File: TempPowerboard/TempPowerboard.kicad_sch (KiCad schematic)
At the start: 0 parts

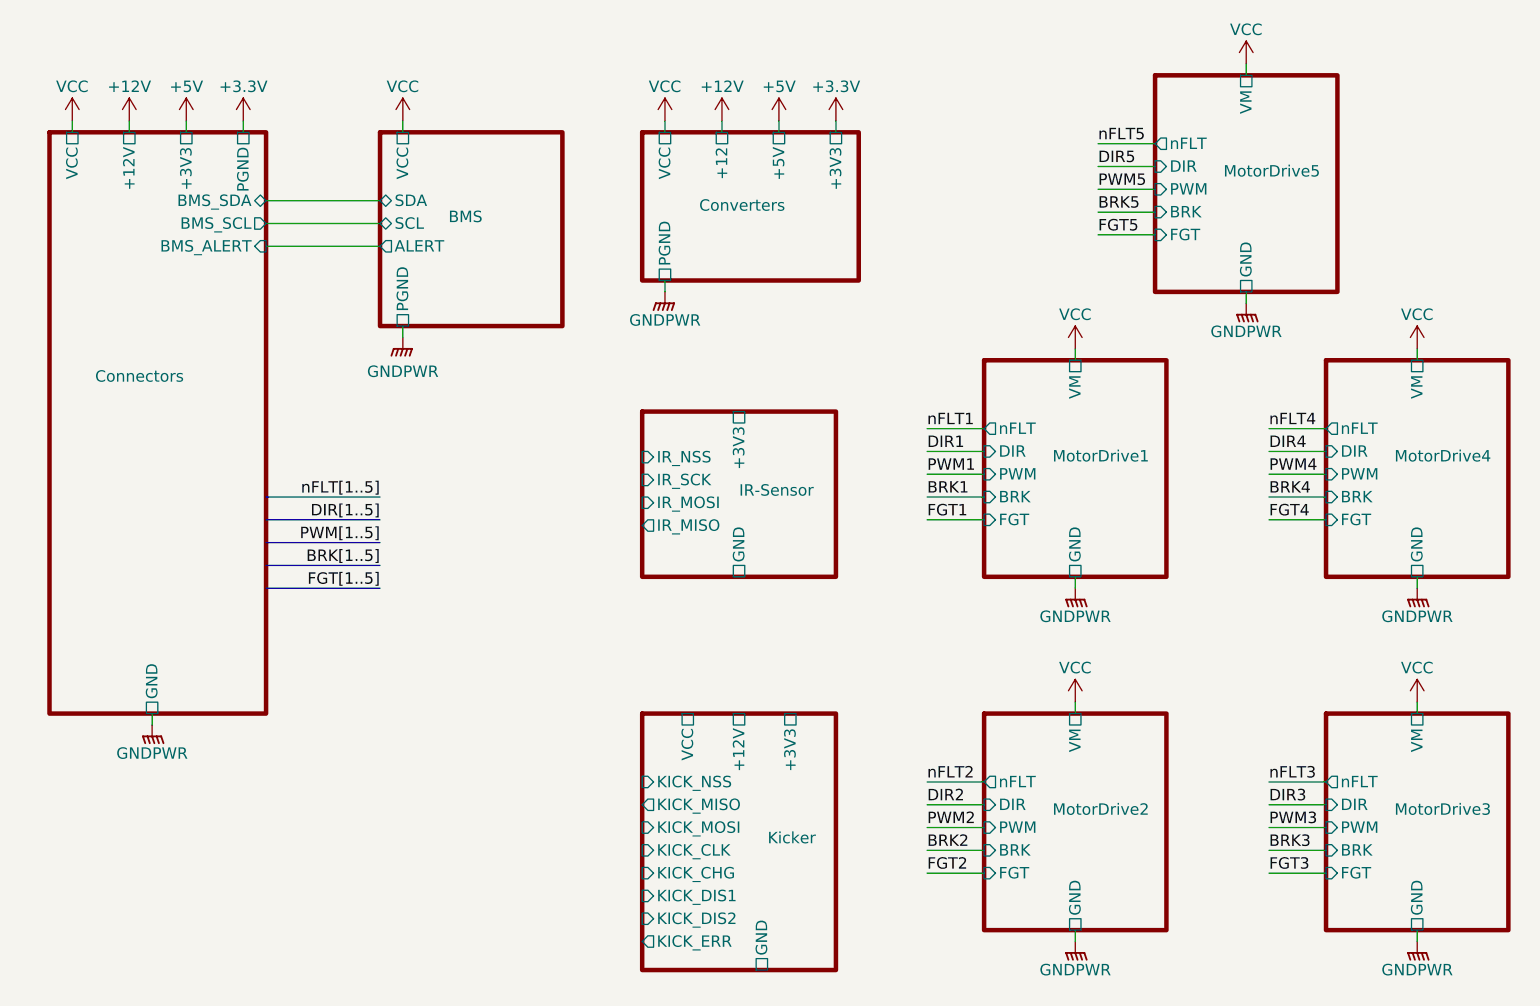
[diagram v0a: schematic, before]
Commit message: Devboard ports defined
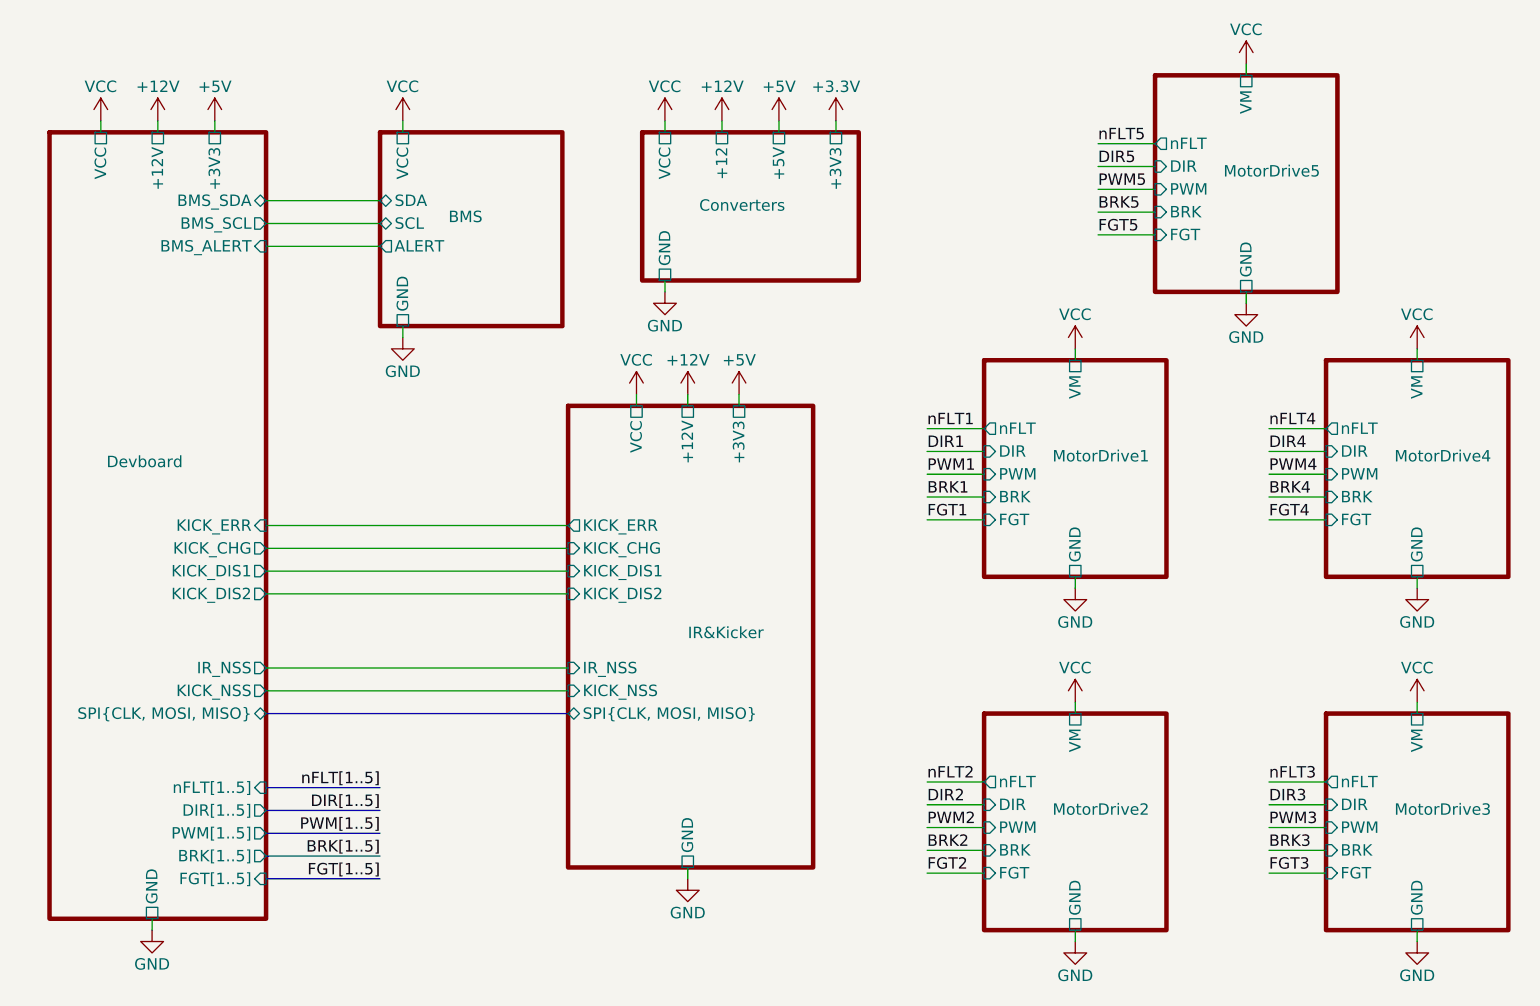
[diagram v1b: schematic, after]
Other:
- sheet Connectors renamed Devboard
- sheet IR-Sensor renamed IR&Kicker
- removed sheet Kicker
- sheet BMS ports: added GND; removed PGND
- sheet Converters ports: added GND; removed PGND
- sheet Devboard ports: added BRK[1..5], DIR[1..5], FGT[1..5], IR_NSS, KICK_CHG, KICK_DIS1, KICK_DIS2, KICK_ERR, KICK_NSS, PWM[1..5], SPI{CLK, MOSI, MISO}, nFLT[1..5]; removed PGND
- sheet IR&Kicker ports: added +12V, KICK_CHG, KICK_DIS1, KICK_DIS2, KICK_ERR, KICK_NSS, SPI{CLK, MOSI, MISO}, VCC; removed IR_MISO, IR_MOSI, IR_SCK
